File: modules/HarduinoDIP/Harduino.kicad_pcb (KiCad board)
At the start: 2 copper layers, 40.6 x 40.6 mm, 42 parts, among them J1 2, J10 11, J11 12, J12 13, J13 A0, J14 A1, J15 A2, J16 A3, J17 A4, J18 A5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

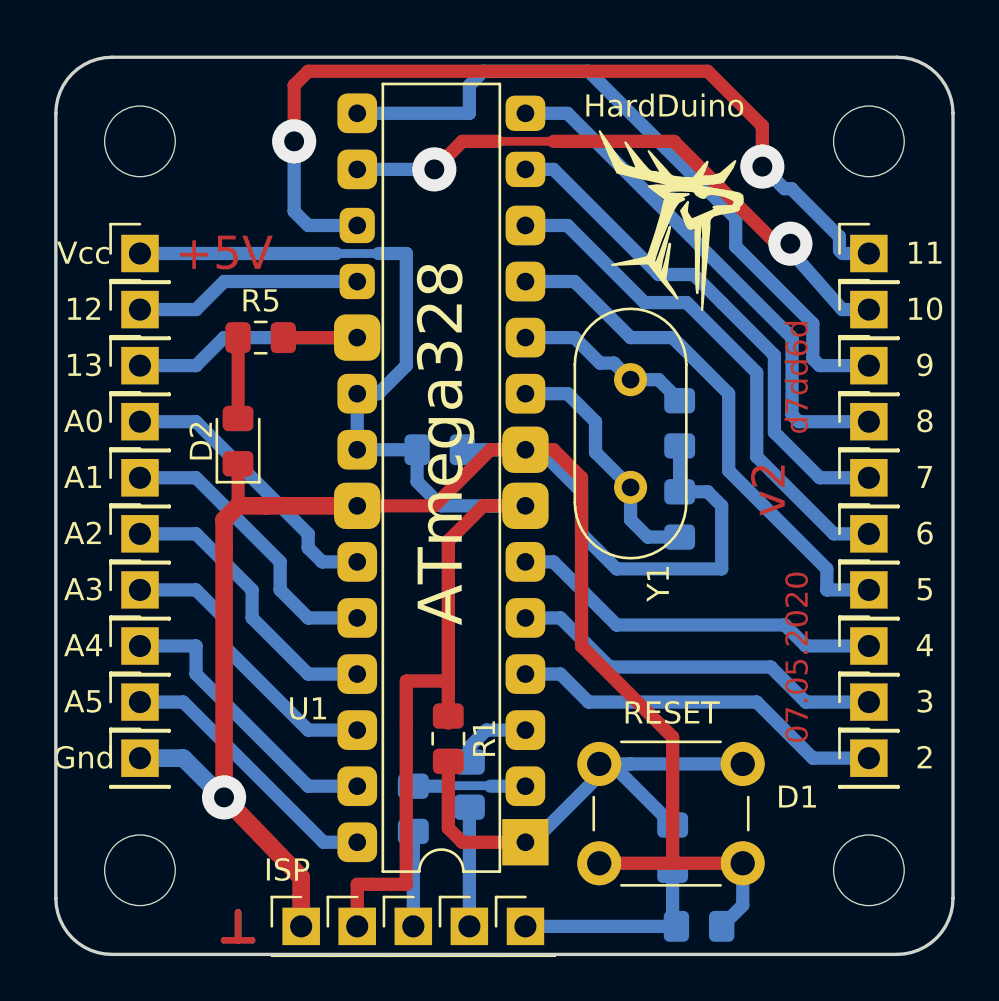
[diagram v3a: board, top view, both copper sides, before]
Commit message: 1x PCBs. Move holes to edges. Caution! This changes is uncompatible with previous versions...
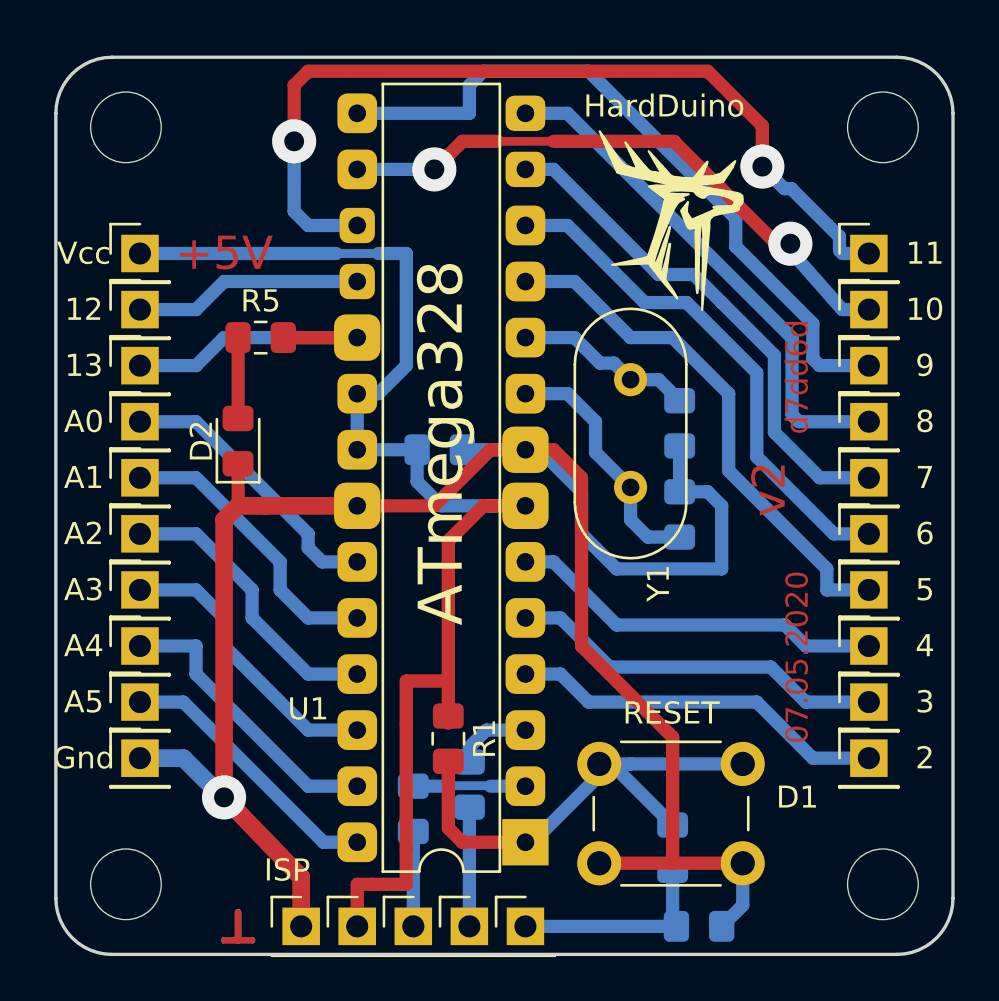
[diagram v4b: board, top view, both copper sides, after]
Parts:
- moved H2 0.90 mm to (86.4, 82.7)
- moved H4 0.90 mm to (120.7, 82.7)
- moved H1 0.90 mm to (86.4, 48.4)
- moved H3 0.90 mm to (120.7, 48.4)
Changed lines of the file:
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@@
   )
   (module MountingHole:MountingHole_3.2mm_M3 (layer F.Cu)
-    (at 87.0585 49.022)
+    (at 86.4235 48.3870)
     (descr "Mounting Hole 3.2mm, no annular, M3")
     (tags "mounting hole 3.2mm no annular m3")
@@
   )
   (module MountingHole:MountingHole_3.2mm_M3 (layer F.Cu)
-    (at 87.0585 82.042)
+    (at 86.4235 82.6770)
     (descr "Mounting Hole 3.2mm, no annular, M3")
     (tags "mounting hole 3.2mm no annular m3")
@@
   )
   (module MountingHole:MountingHole_3.2mm_M3 (layer F.Cu)
-    (at 120.0785 49.022)
+    (at 120.7135 48.3870)
     (descr "Mounting Hole 3.2mm, no annular, M3")
     (tags "mounting hole 3.2mm no annular m3")
@@
   )
   (module MountingHole:MountingHole_3.2mm_M3 (layer F.Cu)
-    (at 120.0785 82.042)
+    (at 120.7135 82.6770)
     (descr "Mounting Hole 3.2mm, no annular, M3")
     (tags "mounting hole 3.2mm no annular m3")

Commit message: Fix hash & version
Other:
- board text added: "21.02.2021"
- board text added: "b4d799"
- board text added: "v2.3"
- board text removed: "07.05.2020"
- board text removed: "d7dd6d"
- board text removed: "v2"

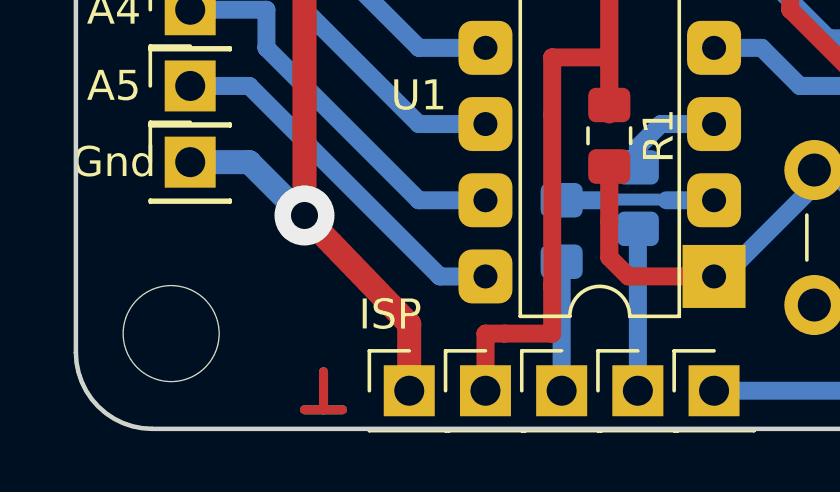
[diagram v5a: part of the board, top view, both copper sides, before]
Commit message: HardDuino. Fix port name.
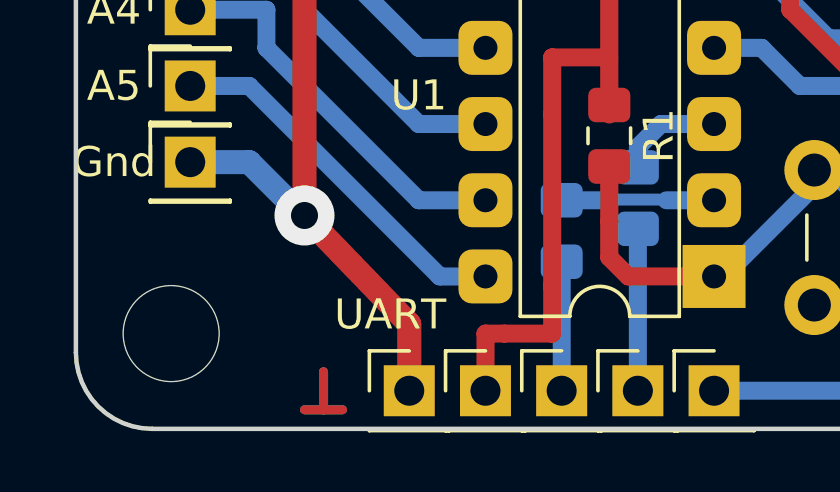
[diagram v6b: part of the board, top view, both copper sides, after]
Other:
- board text added: "UART"
- board text removed: "ISP"

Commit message: Fix hashes
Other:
- board text added: "513641"
- board text removed: "b4d799"

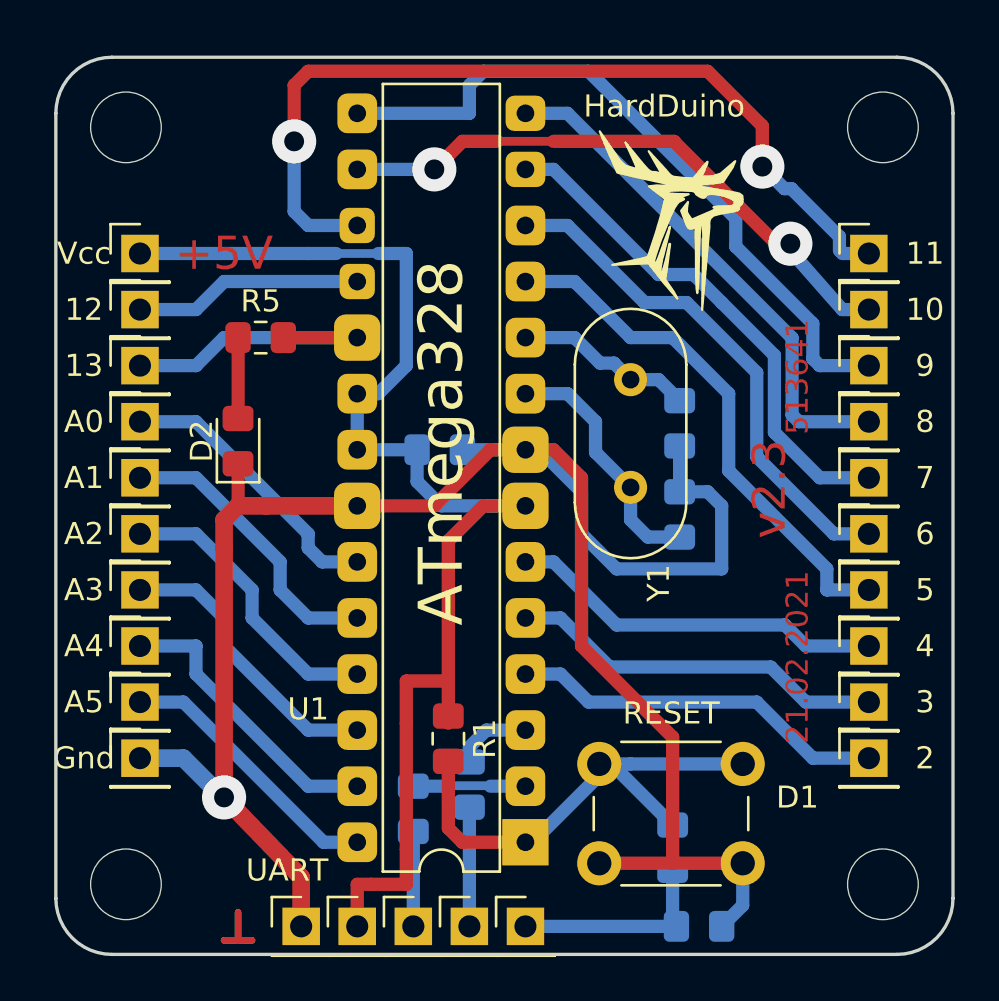
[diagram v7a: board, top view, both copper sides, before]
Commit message: All 1x shields was rotated clockwise
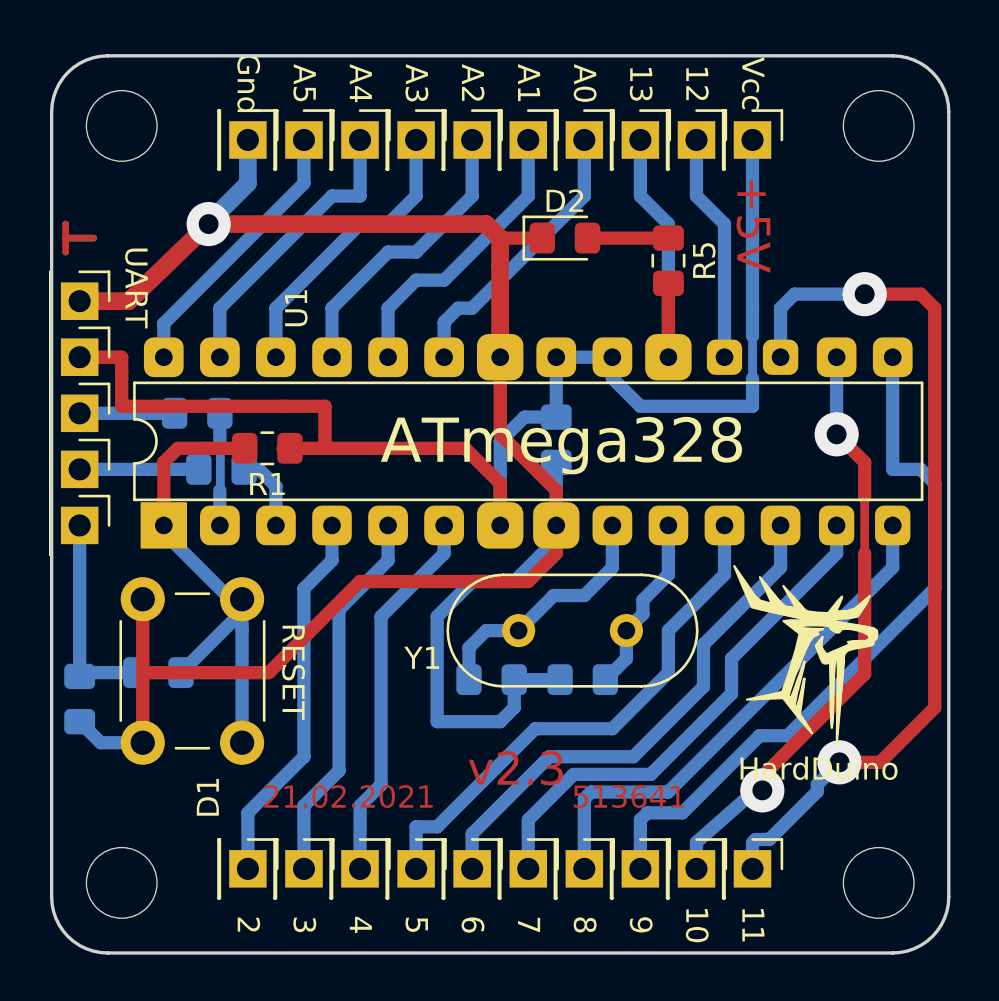
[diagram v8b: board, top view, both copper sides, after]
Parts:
- moved H4 34.5 mm to (86.2, 82.6), turned to 270 degrees
- moved H2 34.4 mm to (86.2, 48.3), turned to 270 degrees
- moved H3 34.2 mm to (120.5, 82.6), turned to 270 degrees
- moved H1 34.1 mm to (120.5, 48.3), turned to 270 degrees
- moved J25 30.0 mm to (84.3, 56.3), turned to 270 degrees
- moved R4 29.9 mm to (84.3, 74.3), turned to 270 degrees
- moved J24 28.7 mm to (84.3, 58.8), turned to 270 degrees
- moved J1 28.6 mm to (91.9, 82.0), turned to 270 degrees
- moved J20 28.4 mm to (91.9, 49.0), turned to 270 degrees
- moved J10 28.4 mm to (114.8, 82.0), turned to 270 degrees
- moved J19 28.2 mm to (114.8, 49.0), turned to 270 degrees
- moved J22 27.7 mm to (84.3, 61.3), turned to 270 degrees
- moved J23 27.2 mm to (84.3, 63.9), turned to 270 degrees
- moved J21 27.2 mm to (84.3, 66.4), turned to 270 degrees
- moved J2 26.7 mm to (94.5, 82.0), turned to 270 degrees
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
